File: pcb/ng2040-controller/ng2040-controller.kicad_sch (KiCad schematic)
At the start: 22 parts, among them J1 A, J2 B, J3 C, J4 D, J5 START, J6 SELECT, J7 JOY, J8 BATTERY, J9 NRF24L01 Connector, SW1 OPTS, SW2 POWER, U1 RP2040-Zero, U2 NRF24L01, U3 MIC5205-3.0YM5

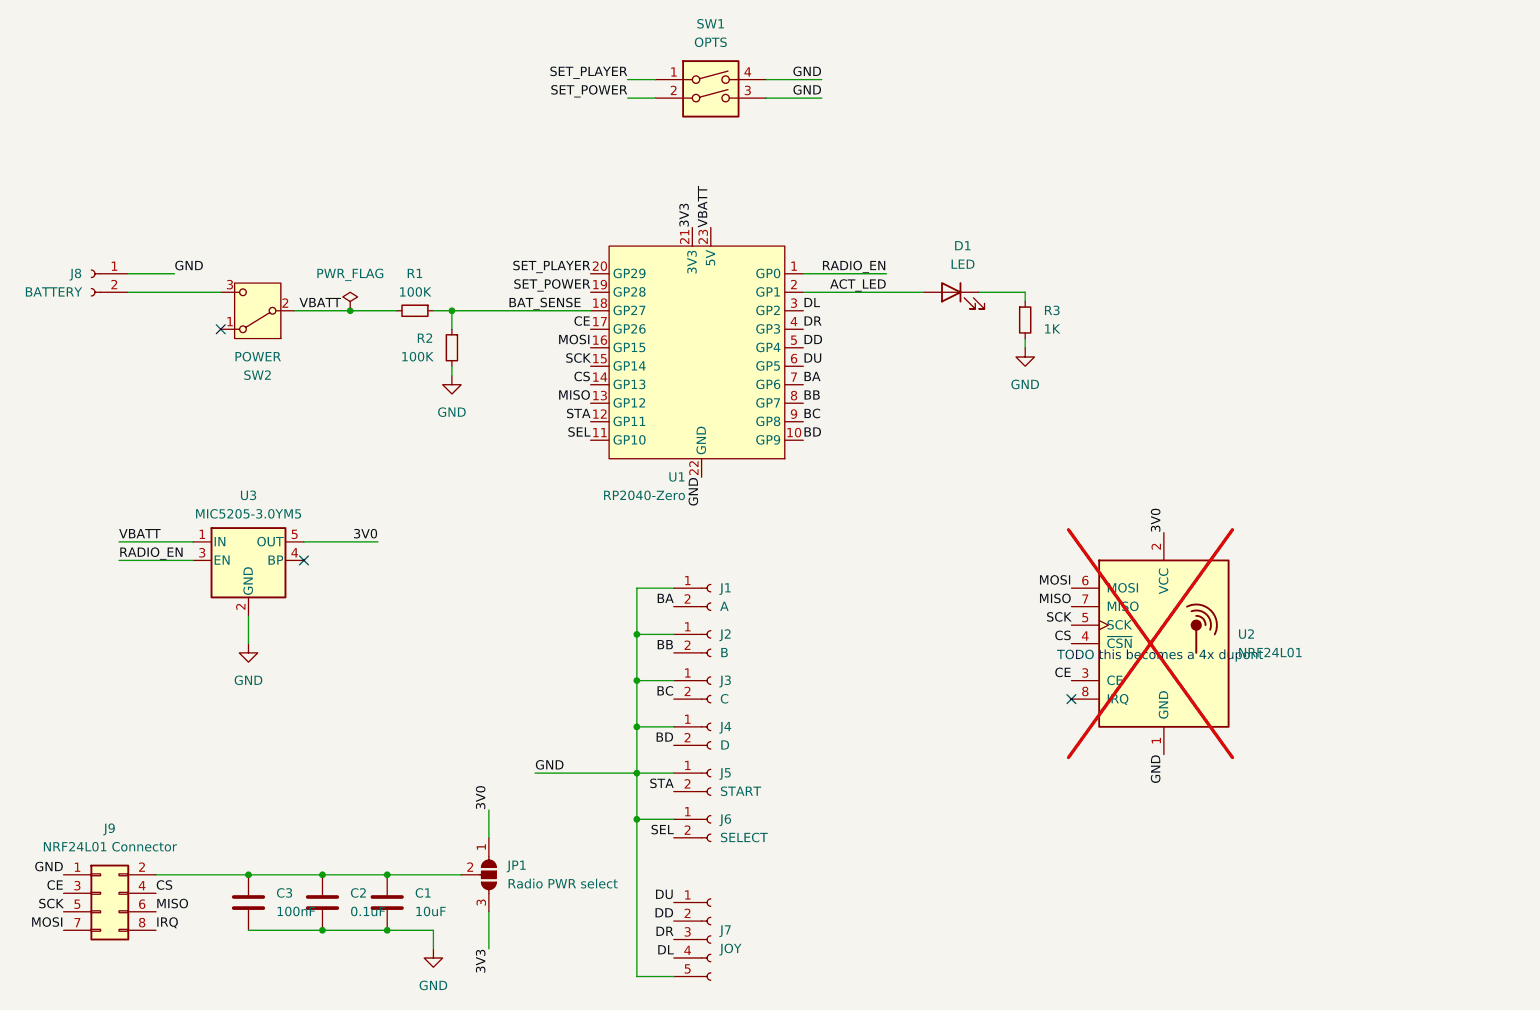
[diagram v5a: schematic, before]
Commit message: Fix issues with REV2
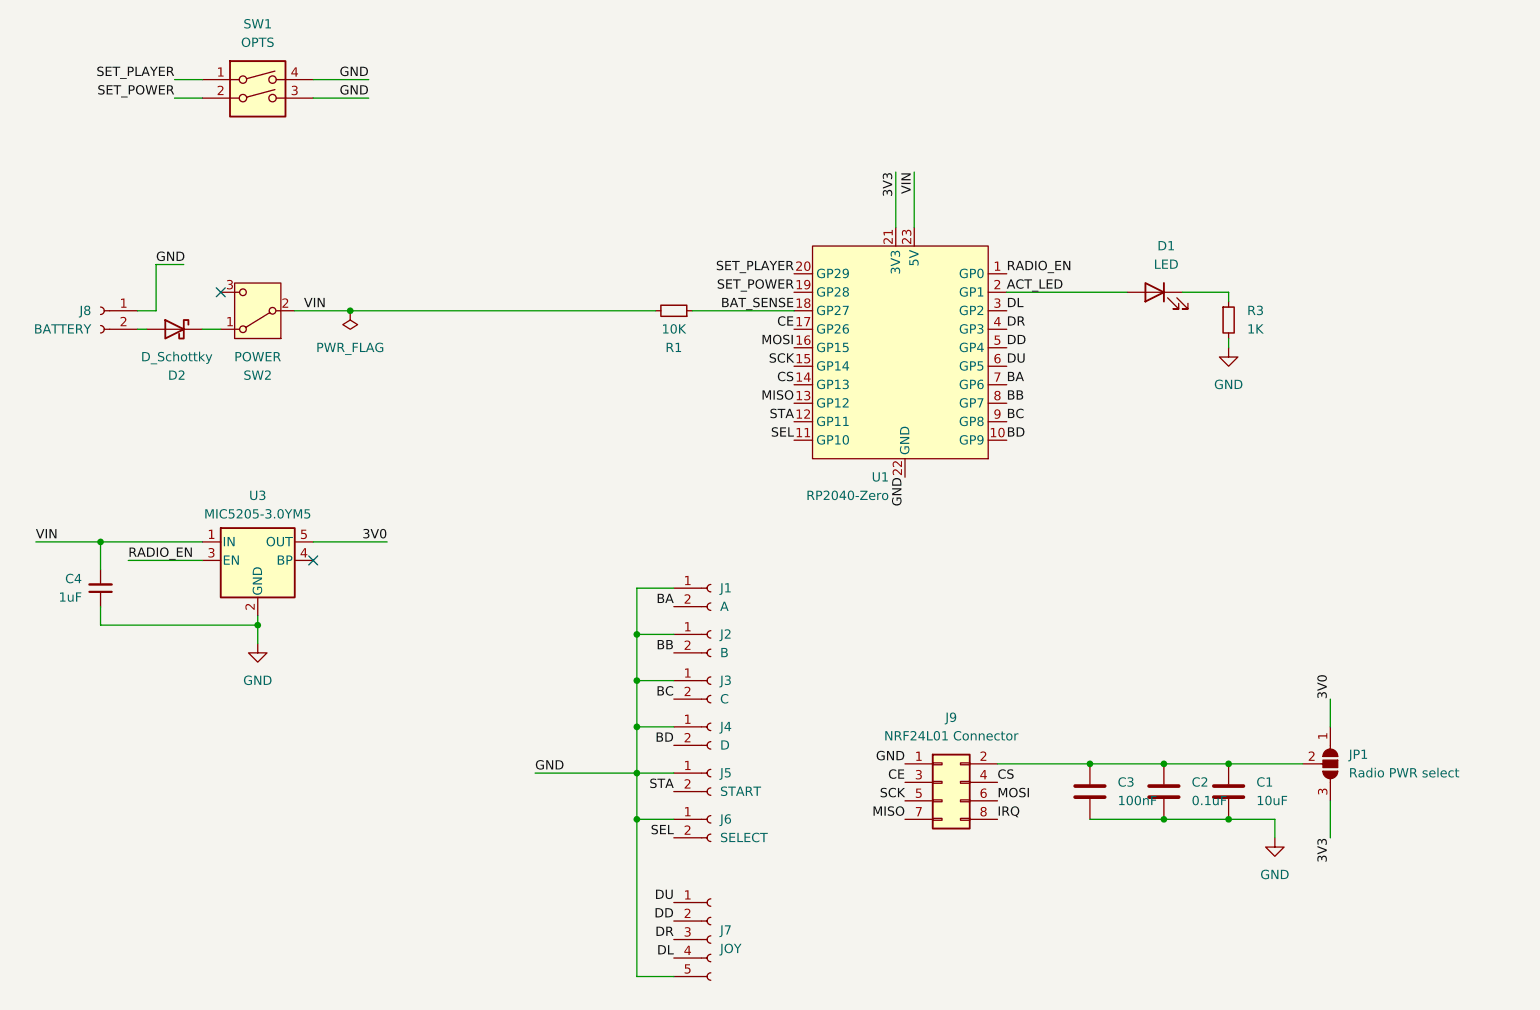
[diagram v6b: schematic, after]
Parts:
- removed R2: 100K, Resistor_SMD:R_0805_2012Metric_Pad1.20x1.40mm_HandSolder, symbol Device:R_Small
- removed U2: NRF24L01, NRF24L01:NRF24L01-SMD, symbol RF:NRF24L01_Breakout
- added C4: 1uF, Capacitor_SMD:C_0805_2012Metric_Pad1.18x1.45mm_HandSolder, symbol Device:C_Small
- added D2: D_Schottky, Diode_SMD:D_SOD-123, symbol Device:D_Schottky
- R1: value 100K -> 10K
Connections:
- net GND: now also C4.1
- net MISO: now also J9.7 (Pin_7); no longer J9.6 (Pin_6)
- net MOSI: now also J9.6 (Pin_6); no longer J9.7 (Pin_7)
- net at SW2.1 (A): now also D2.1 (K)
- net at J8.2 (Pin_2): now also D2.2 (A); no longer SW2.3 (C)
- net VBATT renamed VIN
- net VIN: now also C4.2
- no-connect marks 3 -> 2
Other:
- note removed: "TODO this becomes a 4x dupont"
- moved on the sheet: C1, C2, C3, D1, J8, J9, JP1, R1, R3, SW1, U1, U3

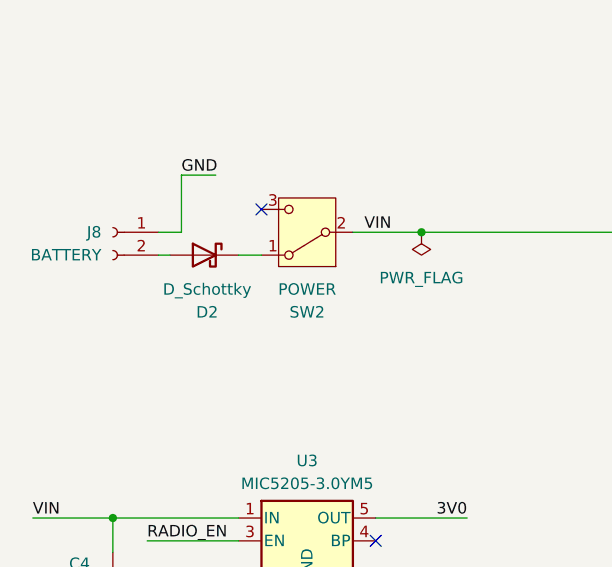
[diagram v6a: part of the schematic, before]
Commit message: Remove diode as we don't want any more voltage drop
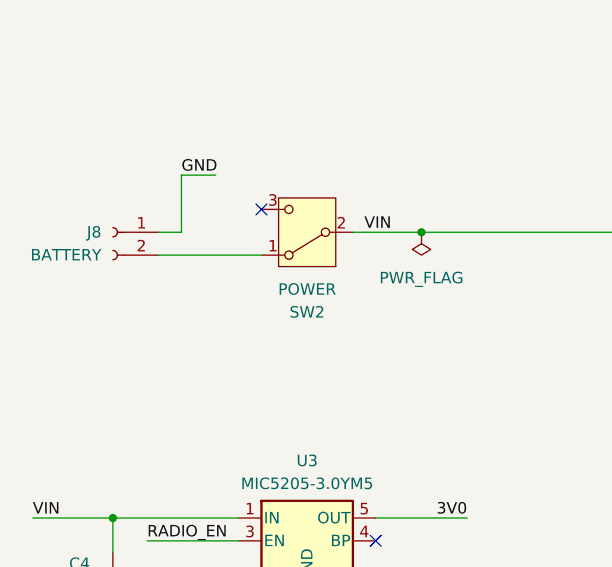
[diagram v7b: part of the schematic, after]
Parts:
- removed D2: D_Schottky, Diode_SMD:D_SOD-123, symbol Device:D_Schottky
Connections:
- net at SW2.1 (A): now also J8.2 (Pin_2)
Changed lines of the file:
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@@
-	(wire
-		(pts
-			(xy 43.18 62.23) (xy 45.72 62.23)
-		)
-		(stroke
-			(width 0)
-			(type default)
-		)
-	)
 	(wire
 		(pts
@@
 	(wire
 		(pts
-			(xy 34.29 62.23) (xy 35.56 62.23)
+			(xy 34.29 62.23) (xy 45.72 62.23)
 		)
 		(stroke
@@
 		)
 	)
-	(symbol
-		(lib_id "Device:D_Schottky")
-		(at 39.37 62.23 0)
-		(mirror y)
-		(unit 1)
-		(exclude_from_sim no)
-		(in_bom yes)
-		(on_board yes)
-		(dnp no)
-		(fields_autoplaced yes)
-		(property "Reference" "D2"
-			(at 39.6875 68.58 0)
-			(effects
-				(font
-					(size 1.27 1.27)
-				)
-			)
-		)
-		(property "Value" "D_Schottky"
-			(at 39.6875 66.04 0)
-			(effects
-				(font
-					(size 1.27 1.27)
-				)
-			)
-		)
-		(property "Footprint" "Diode_SMD:D_SOD-123"
-			(at 39.37 62.23 0)
-			(effects
-				(font
-					(size 1.27 1.27)
-				)
-				(hide yes)
-			)
-		)
-		(property "Datasheet" "~"
-			(at 39.37 62.23 0)
-			(effects
-				(font
-					(size 1.27 1.27)
-				)
-				(hide yes)
-			)
-		)
-		(property "Description" "Schottky diode"
-			(at 39.37 62.23 0)
-			(effects
-				(font
-					(size 1.27 1.27)
-				)
-				(hide yes)
-			)
-		)
-		(pin "2"
-		)
-		(pin "1"
-		)
-		(instances
-			(project "ng2040-controller"
-				(path "/e91880d7-e1f1-43ba-b9bf-5f0fc90655d2"
-					(reference "D2")
-					(unit 1)
-				)
-			)
-		)
-	)

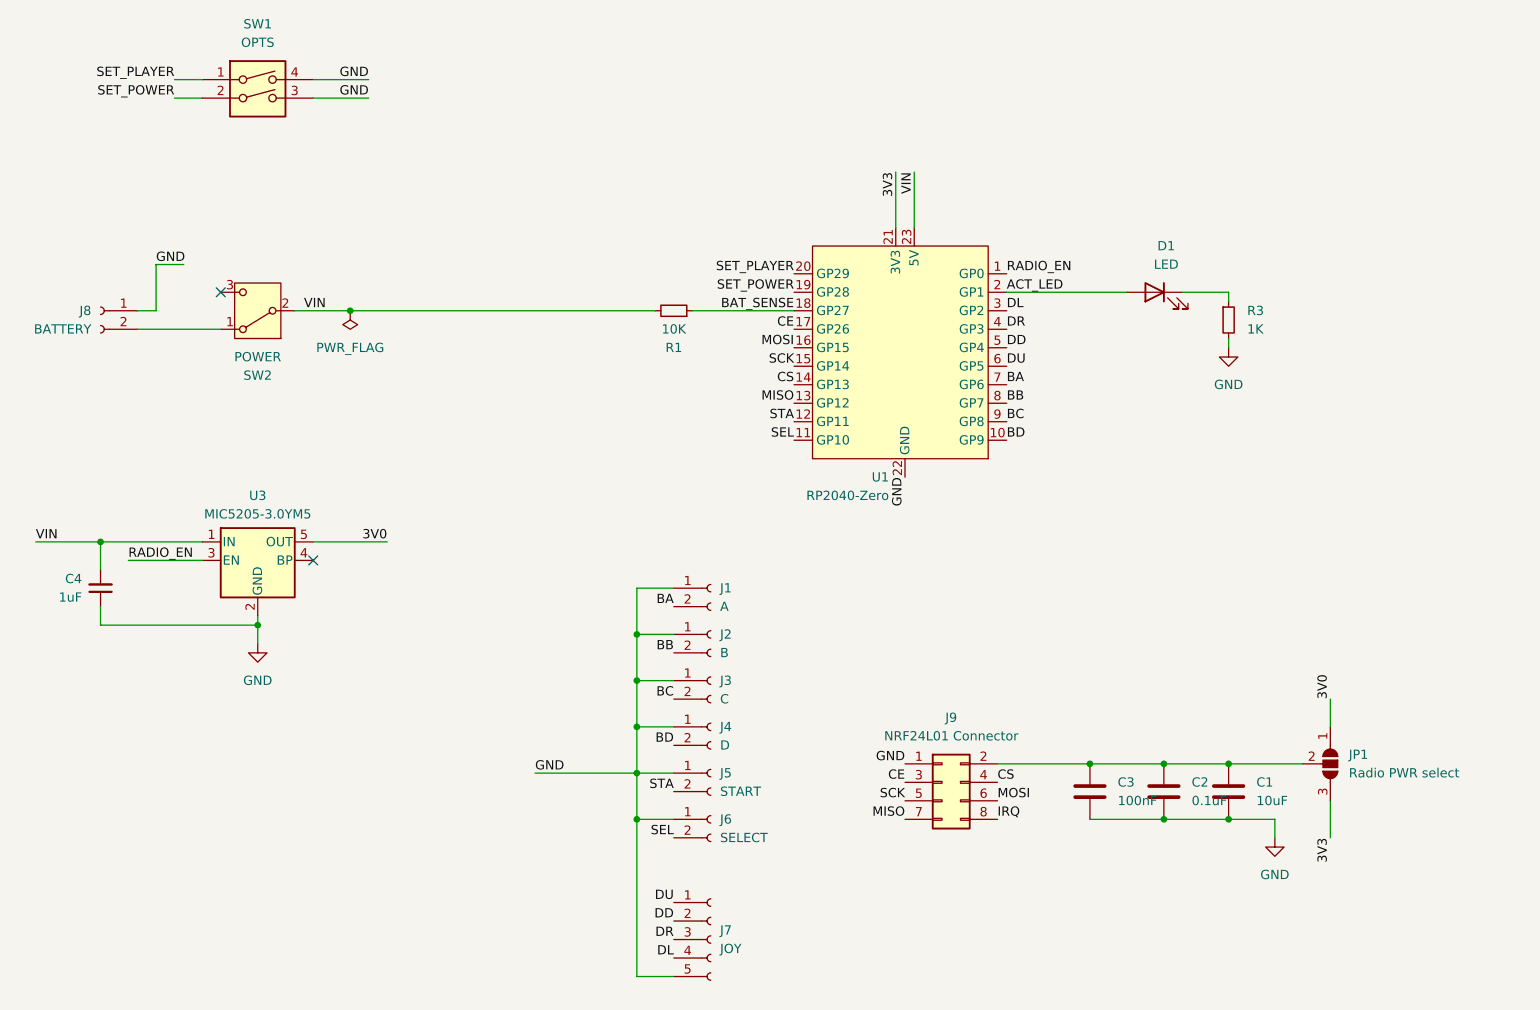
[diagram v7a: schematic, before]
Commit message: WIP: put LED on analog pin to modulate brightness, need to relayout
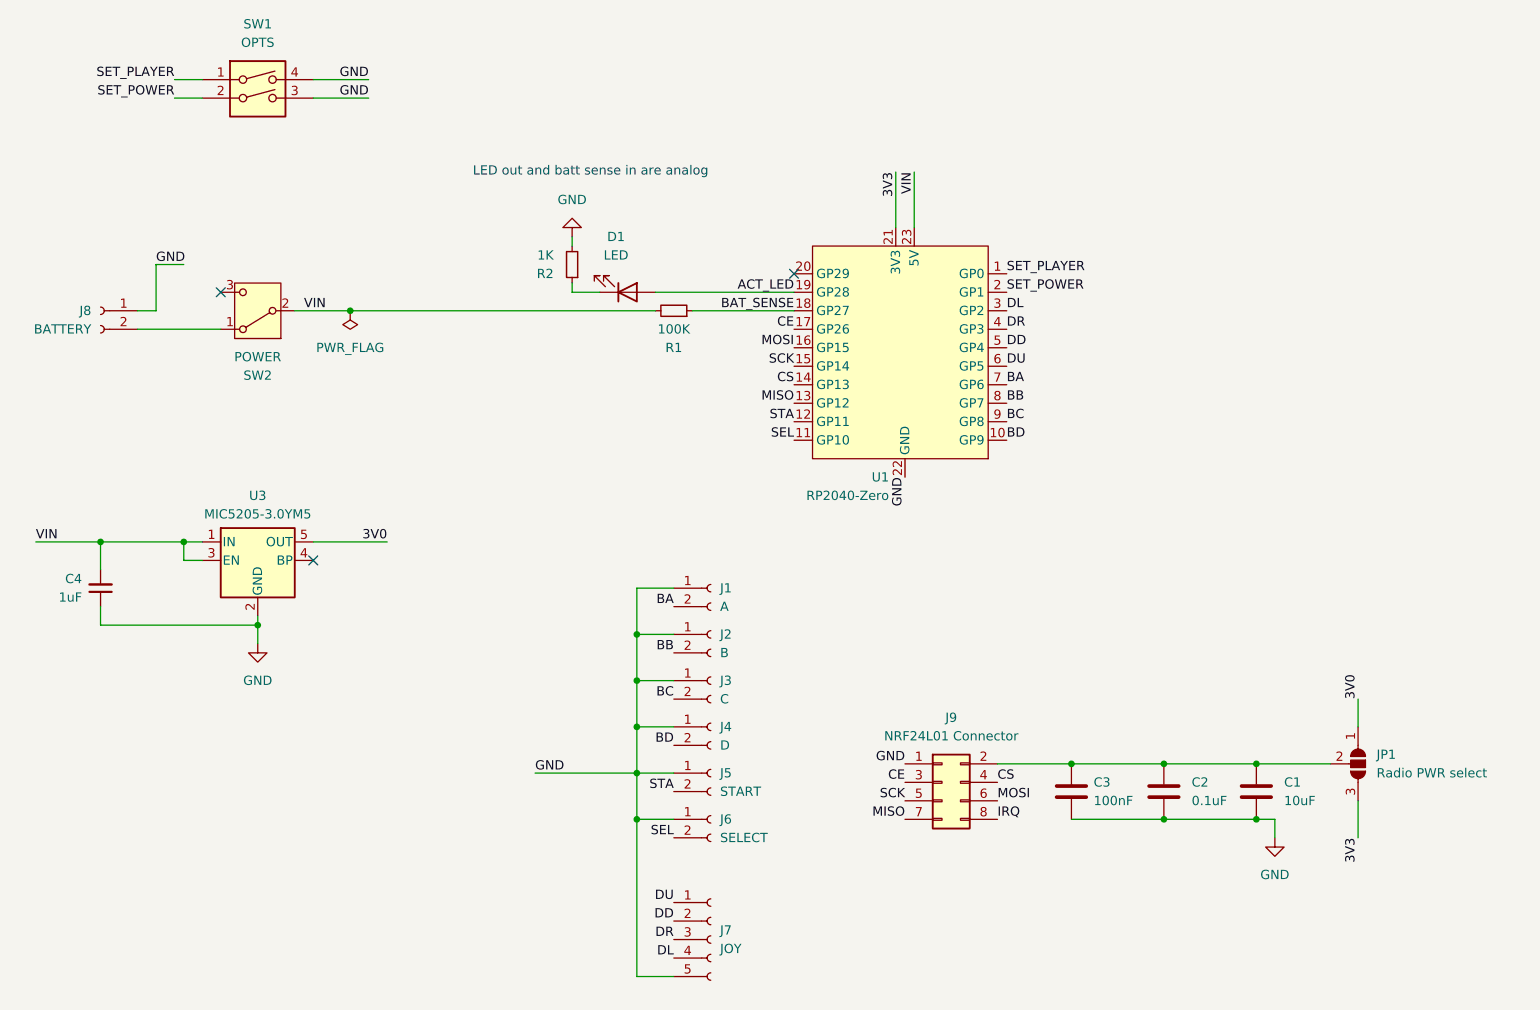
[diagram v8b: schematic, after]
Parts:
- removed R3: 1K, Resistor_SMD:R_0805_2012Metric_Pad1.20x1.40mm_HandSolder, symbol Device:R_Small
- added R2: 1K, Resistor_SMD:R_0805_2012Metric_Pad1.20x1.40mm_HandSolder, symbol Device:R_Small
- R1: value 10K -> 100K
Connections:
- net ACT_LED: now also U1.19 (GP28); no longer U1.2 (GP1)
- net GND: now also R2.2
- net SET_PLAYER: now also U1.1 (GP0); no longer U1.20 (GP29)
- net SET_POWER: now also U1.2 (GP1); no longer U1.19 (GP28)
- net VIN: now also U3.3 (EN)
- net at D1.1 (K): now also R2.1
- removed net RADIO_EN: U1.1 (GP0), U3.3 (EN)
- no-connect marks 2 -> 3
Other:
- note added: "LED out and batt sense in are analog"
- moved on the sheet: C1, C3, JP1
